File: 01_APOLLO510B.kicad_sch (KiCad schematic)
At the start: 0 parts

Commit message: fixed schematics errors
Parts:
- added C101, C102, C103, C104: 4.7uF, Capacitor_SMD:C_0201_0603Metric, symbol Device:C
- added C105: 10uF, Capacitor_SMD:C_0402_1005Metric, symbol Device:C
- added C106: 1uF, Capacitor_SMD:C_0402_1005Metric, symbol Device:C
- added C107, C108, C109, C112, C114, C117: 2.2uF, Capacitor_SMD:C_0402_1005Metric, symbol Device:C
- added C110: 4.7uF, Capacitor_SMD:C_0402_1005Metric, symbol Device:C
- added C111, C113, C115, C120, C121, C122, C123, C124, C125, C126, C127: 100nF, Capacitor_SMD:C_0402_1005Metric, symbol Device:C
- added C116: 1.0uF, Capacitor_SMD:C_0402_1005Metric, symbol Device:C
- added C118, C119: TBD <=10pF, Capacitor_SMD:C_0201_0603Metric, symbol Device:C
- added C128: 100pF, Capacitor_SMD:C_0201_0603Metric, symbol Device:C
- added L101: 2.2uH / Isat>=1A / DCR<550mR, symbol sportwatch_custom:INDUCTOR_2PIN
- added R101: 10M, Resistor_SMD:R_0402_1005Metric, symbol Device:R
- added R102, R103: 100k, Resistor_SMD:R_0402_1005Metric, symbol Device:R
- added R104, R105, R106, R107: 4.7k, Resistor_SMD:R_0402_1005Metric, symbol Device:R
- added R108: 200k, Resistor_SMD:R_0402_1005Metric, symbol Device:R
- added R109: 300k, Resistor_SMD:R_0402_1005Metric, symbol Device:R
- added R110: 10k, Resistor_SMD:R_0402_1005Metric, symbol Device:R
- added R111: 22R initial, Resistor_SMD:R_0201_0603Metric, symbol Device:R
- added U101: AP510BFA-CBR, symbol sportwatch_custom:AP510BFA-CBR
- added U102: SN74AXC8T245, symbol sportwatch_custom:SN74AXC8T245
- added U103: TXB0101DRLR, symbol sportwatch_custom:TXB0101
- added U104, U105: SN74AXC1T45, symbol sportwatch_custom:SN74AXC1T45
- added U106: PCA9306DCU, Package_SO:VSSOP-8_3.0x3.0mm_P0.65mm, symbol sportwatch_custom:PCA9306DCU
- added Y101: 32.768kHz / low-CL TBD, symbol sportwatch_custom:XTAL_2PIN
- added Y102: 48MHz / CL=8-11pF / ESR<=60R, symbol sportwatch_custom:XTAL_2PIN
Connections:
- new net ALS_INT: U101.J3 (GPIO36)
- new net APOLLO_BLE_ANT: U101.N1 (BLE_ANT)
- new net APOLLO_BLE_AVDD_PA: U101.M1 (BLE_AVDD_PA)
- new net APOLLO_BLE_ENABLE: R101.1, U101.E5 (BLE_ENABLE)
- new net APOLLO_BLE_VBAT1: C117.1, U101.A8 (BLE_VBAT1)
- new net APOLLO_BLE_XIN: U101.N6 (BLE_XIN), Y102.1 (X1)
- new net APOLLO_BLE_XOUT: U101.N7 (BLE_XOUT), Y102.2 (X2)
- new net APOLLO_LPADC_VREF: C113.1, U101.A13 (LPADC_VREF)
- new net APOLLO_LPMICBIAS: C114.1, U101.B11 (LPMICBIAS)
- new net APOLLO_RST_N: U101.H4 (RSTN)
- new net APOLLO_SIMOBUCK_SW: L101.1, U101.A1 (SIMOBUCK_SW)
- new net APOLLO_SIMOBUCK_SWSEL: L101.2, U101.A2 (SIMOBUCK_SWSEL)
- new net APOLLO_SWCLK: U101.M3 (GPIO20)
- new net APOLLO_SWDIO: U101.N3 (GPIO21)
- new net APOLLO_SWO_GPIO28: U101.L1 (GPIO28)
- new net APOLLO_VDDC: C101.1, U101.A3 (VDDC)
- new net APOLLO_VDDC_LV: C102.1, U101.B3 (VDDC_LV)
- new net APOLLO_VDDF: C103.1, U101.C2 (VDDF)
- new net APOLLO_VDDS: C104.1, U101.C1 (VDDS)
- new net APOLLO_XI32: C118.1, U101.B5 (XI), Y101.1 (X1)
- new net APOLLO_XO32: C119.1, U101.A4 (XO), Y101.2 (X2)
- new net BARO_INT: U101.F13 (GPIO37)
- new net BTN_BACK_N: U101.F11 (GPIO39)
- new net BTN_DOWN_N: U101.C4 (GPIO19)
- new net BTN_LIGHT_N: U101.G5 (GPIO17)
- new net BTN_START_N: U101.G13 (GPIO38)
- new net BTN_UP_N: U101.F5 (GPIO18)
- new net DISP_LS_OE_N: R102.2, U101.H1 (GPIO95), U102.22 (~{OE})
- new net DISP_QSPI_CLK: U102.21 (B1)
- new net DISP_QSPI_CS: U102.20 (B2)
- new net DISP_QSPI_IO0: U103.4 (B)
- new net DISP_QSPI_IO0_OE: R103.1, U101.H2 (GPIO96), U103.5 (OE)
- new net DISP_QSPI_IO1: U102.19 (B3)
- new net DISP_QSPI_IO2: U102.18 (B4)
- new net DISP_QSPI_IO3: U102.17 (B5)
- new net DISP_RST: U102.16 (B6)
- new net DISP_TE: U104.4 (B)
- new net DISP_VCI_EN: U102.15 (B7)
- new net EMMC_CLK: R111.2
- new net EMMC_CMD: U101.K8 (GPIO160)
- new net EMMC_DAT0: U101.H10 (GPIO84)
- new net EMMC_DAT1: U101.J10 (GPIO85)
- new net EMMC_DAT2: U101.K10 (GPIO86)
- new net EMMC_DAT3: U101.L9 (GPIO87)
- new net EMMC_DAT4: U101.H7 (GPIO156)
- new net EMMC_DAT5: U101.J7 (GPIO157)
- new net EMMC_DAT6: U101.K7 (GPIO158)
- new net EMMC_DAT7: U101.L8 (GPIO159)
- new net EMMC_RST_N: U101.C10 (GPIO51)
- new net ENV_I2C_SCL: U101.K3 (GPIO34)
- new net ENV_I2C_SDA: U101.J4 (GPIO35)
- new net GND: C101.2, C102.2, C103.2, C104.2, C105.2, C106.2, C107.2, C108.2, C109.2, C110.2, C111.2, C112.2, C113.2, C114.2, C115.2, C116.2, C117.2, C118.2, C119.2, C120.2, C121.2, C122.2, C123.2, C124.2, C125.2, C126.2, C127.2, C128.2, R101.2, R103.2, R109.2, U101.A6 (BLE_VSS_DCDC), U101.A7 (BLE_SW_DCDC), U101.B2 (VSSP), U101.B4 (VSSA), U101.C12 (VSSAUDA), U101.E1 (BLE_VSS1), U101.K11 (VSS), U101.L10 (VDDUSB0P9), U101.M2 (BLE_AVSS_ANT), U101.N10 (VSSAUSB), U101.N11 (VDD18), U101.N12 (VSS18), U101.N2 (BLE_AVSS_RF), U101.N9 (VDDUSB33), U102.12 (GND1), U102.13 (GND2), U103.2 (GND), U104.2 (GND), U104.5 (DIR), U105.2 (GND), U105.5 (DIR), U106.1 (GND)
- new net GNSS_EXTINT: U101.G12 (GPIO43)
- new net GNSS_TIMEPULSE: U101.E11 (GPIO45)
- new net GNSS_UART_RX: U101.C11 (GPIO46)
- new net GNSS_UART_TX: U101.F12 (GPIO44)
- new net HAPTIC_I2C_SCL: U101.K1 (GPIO47)
- new net HAPTIC_I2C_SDA: U101.J2 (GPIO48)
- new net HAPTIC_NRST: U101.J1 (GPIO49)
- new net HAPTIC_TRIG_INTZ: U101.D10 (GPIO57)
- new net IMU_INT1: U101.D7 (GPIO14)
- new net IMU_INT2: U101.H5 (GPIO16)
- new net IMU_SPI_CS: U101.D6 (GPIO11)
- new net IMU_SPI_MISO: U101.C6 (GPIO10)
- new net IMU_SPI_MOSI: U101.B6 (GPIO9)
- new net IMU_SPI_SCK: U101.D5 (GPIO8)
- new net MAG_I2C_SCL: U101.L6 (GPIO5)
- new net MAG_I2C_SDA: U101.K6 (GPIO6)
- new net MAG_INT: U101.J6 (GPIO7)
- new net MCU_DISP_QSPI_CLK_1V8: U101.D4 (GPIO102), U102.3 (A1)
- new net MCU_DISP_QSPI_CS_1V8: U101.F4 (GPIO99), U102.4 (A2)
- new net MCU_DISP_QSPI_IO0_1V8: U101.G3 (GPIO100), U103.3 (A)
- new net MCU_DISP_QSPI_IO1_1V8: U101.E4 (GPIO101), U102.5 (A3)
- new net MCU_DISP_QSPI_IO2_1V8: U101.F3 (GPIO103), U102.6 (A4)
- new net MCU_DISP_QSPI_IO3_1V8: U101.C3 (GPIO104), U102.7 (A5)
- new net MCU_DISP_RST_1V8: U101.L11 (GPIO83), U102.8 (A6)
- new net MCU_DISP_TE_1V8: U101.D11 (GPIO50), U104.3 (A)
- new net MCU_DISP_VCI_EN_1V8: U101.H3 (GPIO98), U102.9 (A7)
- new net MCU_EMMC_CLK: R111.1, U101.K9 (GPIO88)
- new net MCU_TOUCH_INT_1V8: U101.K2 (GPIO33), U105.3 (A)
- new net MCU_TOUCH_RST_1V8: U101.E10 (GPIO41), U102.10 (A8)
- new net MCU_TOUCH_SCL_1V8: R104.2, U101.K4 (GPIO31), U106.3 (SCL1)
- new net MCU_TOUCH_SDA_1V8: R105.2, U101.L3 (GPIO32), U106.4 (SDA1)
- new net PPG1_CS_N: U101.D9 (GPIO24)
- new net PPG1_INT_N: U101.D8 (GPIO22)
- new net PPG2_CS_N: U101.M5 (GPIO29)
- new net PPG2_INT_N: U101.C8 (GPIO23)
- new net PPG_SAMPLE_SYNC: U101.H13 (GPIO42)
- new net PPG_SPI_MISO: U101.L7 (GPIO27)
- new net PPG_SPI_MOSI: U101.L5 (GPIO26)
- new net PPG_SPI_SCLK: U101.K5 (GPIO25)
- new net SYS_3V3: C121.1, C123.1, C125.1, C127.1, R106.1, R107.1, R108.1, R110.1, U102.23 (VCCB1), U102.24 (VCCB2), U103.6 (VCCB), U104.6 (VCCB), U105.6 (VCCB)
- new net TOUCH_I2C_VREF2: C128.1, R108.2, U106.7 (VREF2), U106.8 (EN)
- new net TOUCH_INT: R110.2, U105.4 (B)
- new net TOUCH_RST: U102.14 (B8)
- new net TOUCH_SCL: R106.2, U106.6 (SCL2)
- new net TOUCH_SDA: R107.2, U106.5 (SDA2)
- new net VOUT1_1V8: C105.1, C106.1, C107.1, C108.1, C109.1, C110.1, C111.1, C112.1, C115.1, C116.1, C120.1, C122.1, C124.1, C126.1, R102.1, R104.1, R105.1, R109.1, U101.B1 (VDDP), U101.B12 (VDDAUDA), U101.B13 (VDDH), U101.C13 (VDDH2), U101.C5 (VDDA), U101.D1 (VDDH1), U101.E13 (BLE_VIO), U101.F1 (BLE_VCC), U101.G1 (BLE_VBAT2), U101.G10 (VDDH4), U101.H12 (VDDH3), U102.1 (VCCA), U102.11 (DIR2), U102.2 (DIR1), U103.1 (VCCA), U104.1 (VCCA), U105.1 (VCCA), U106.2 (VREF1)
- new net WIFI_BUCKEN: U101.F10 (GPIO69)
- new net WIFI_COEX_GRANT: U101.D13 (GPIO40)
- new net WIFI_COEX_REQ: U101.G11 (GPIO73)
- new net WIFI_COEX_STATUS: U101.K12 (GPIO71)
- new net WIFI_HOST_IRQ: U101.M12 (GPIO68)
- new net WIFI_IOVDD_EN: U101.J11 (GPIO70)
- new net WIFI_QSPI_CLK: U101.M11 (GPIO72)
- new net WIFI_QSPI_CS: U101.D12 (GPIO199)
- new net WIFI_QSPI_IO0: U101.H11 (GPIO64)
- new net WIFI_QSPI_IO1: U101.J13 (GPIO65)
- new net WIFI_QSPI_IO2: U101.L12 (GPIO66)
- new net WIFI_QSPI_IO3: U101.J12 (GPIO67)
- no-connect marks 0 -> 36
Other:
- note added: "01_APOLLO510B — SYSTEM MCU / FINAL SIGNAL ALLOCATION — REV A"
- note added: "32.768kHz crystal is kept for accurate RTC/timekeeping; exact crystal + load caps are selected in BOM/footprint pass. 48MHz BLE crystal uses on-chip tuning; no external load caps shown."
- note added: "All VDDP/VDDA/VDDH rails are 1.8V. VDDH1-4 are also 1.8V so every unshifted peripheral bus is 1.8V. SYS_3V3 is only used on the display/touch side of translators."
- note added: "BLE CONTROLLER — VOLTAGE MULTIPLIER MODE @ 1.8V"
- note added: "BLE controller is voltage-multiplier mode: A7 BLE_SW_DCDC grounded; VIO/VBAT2/VCC=1.8V; A8 VBAT1 has 2.2uF. This avoids a second BLE DCDC inductor."
- note added: "BLE_SW_DCDC is grounded in voltage-multiplier mode. BLE_VBAT2, BLE_VCC and BLE_VIO are all 1.8V; BLE_ENABLE E5 has the required ~10M pull-down."
- note added: "C105=VDDP 10uF; C106=VDDA 1uF; C107=VDDH 2.2uF; C108=VDDH1 2.2uF; C109=VDDH2 2.2uF; C110=VDDH3 4.7uF; C111=VDDH4 100nF; C112=VDDAUDA 2.2uF."
- note added: "CO5300 command reads return on QSPI SIO0. U103 is TXB0101 auto-direction; 1.8V-side max data rate is 60Mbps versus CO5300 max 50MHz QSPI write clock / 10MHz read clock."
- note added: "DISPLAY + TOUCH LEVEL TRANSLATION — REQUIRED: APOLLO GPIO=1.8V, SELECTED MODULE I/O=3.3V"
- note added: "Display uses dedicated DISP_QSPI functions on GPIO100-104, GPIO83 reset, GPIO50 TE, GPIO99 CS (GPIO), GPIO98 VCI_EN. GPIO96 controls U103 OE; GPIO95 controls U102 OE."
- note added: "GPIO15/J5 is internally used as BLE reference clock and is NC. RESERVED balls H8/H9/J8/J9/M7/M8 are NC. USB data/MIPI pads are NC; unused USB/MIPI supply rails are grounded per Ambiq guidance."
- note added: "Native KiCad ERC must be run after final hierarchical export because child-sheet labels are not cross-sheet connections yet."
- note added: "PIN MUX: eMMC reserves SDIF0 GPIO84-88 + GPIO156-160; do not reassign. R111 is at Apollo end of CLK."
- note added: "POWER / SIMO / CLOCK SUPPORT"
- note added: "R111 is the eMMC clock source terminator and belongs physically next to Apollo GPIO88; 22R is an initial SI value."
- note added: "Selected ZC-A1D43W-046 module specifies 3.3V QSPI and touch I/O. Apollo GPIO rails are 1.8V here, so level translation is mandatory. Keep 03_DISPLAY R301/R302 DNP because U106 block provides high-side I2C pull-ups."
- note added: "U101 pin map = exact AP510BFA-CBR 153-ball package. Gray/unpopulated package positions are omitted; RESERVED balls and GPIO15 are explicitly NC."
- note added: "Wi-Fi uses MSPI0 GPIO64-73 plus GPIO199 CS; all on 1.8V VDDH3 domain. nRF7002 IOVDD is also 1.8V."
- title: (none) -> Rev-A — Apollo510B MCU / System Integration

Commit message: refactor(kicad): integrate Rev-A hierarchy and libraries
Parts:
- U106: footprint Package_SO:VSSOP-8_3.0x3.0mm_P0.65mm -> Package_SO:VSSOP-8_2.3x2mm_P0.5mm

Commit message: feat(kicad): assign and audit Rev-A footprints
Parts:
- L101: footprint (none) -> Inductor_SMD:L_0603_1608Metric
- U101: footprint (none) -> sportwatch_custom:BGA-153_5.6x5.6mm_Layout13x13_P0.4mm_Ball0.25mm_Pad0.22mm_NSMD
- U102: footprint (none) -> sportwatch_custom:Texas_RHL0024A
- U103, U104, U105: footprint (none) -> Package_TO_SOT_SMD:SOT-563
- Y101: footprint (none) -> Crystal:Crystal_SMD_2012-2Pin_2.0x1.2mm
- Y102: footprint (none) -> sportwatch_custom:Crystal_1612-2Pin_1.6x1.2mm
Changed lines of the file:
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@@
 			)
 		)
-		(property "Footprint" ""
+		(property "Footprint" "sportwatch_custom:BGA-153_5.6x5.6mm_Layout13x13_P0.4mm_Ball0.25mm_Pad0.22mm_NSMD"
 			(at 153 148 0)
 			(hide yes)
@@
 			)
 		)
-		(property "Footprint" ""
+		(property "Footprint" "Package_TO_SOT_SMD:SOT-563"
 			(at 400 222 0)
 			(hide yes)
@@
 			)
 		)
-		(property "Footprint" ""
+		(property "Footprint" "Package_TO_SOT_SMD:SOT-563"
 			(at 350 222 0)
 			(hide yes)
@@
 			)
 		)
-		(property "Footprint" ""
+		(property "Footprint" "Package_TO_SOT_SMD:SOT-563"
 			(at 300 222 0)
 			(hide yes)
@@
 			)
 		)
-		(property "Footprint" ""
+		(property "Footprint" "Inductor_SMD:L_0603_1608Metric"
 			(at 285 30 0)
 			(hide yes)
@@
 			)
 		)
-		(property "Footprint" ""
+		(property "Footprint" "sportwatch_custom:Crystal_1612-2Pin_1.6x1.2mm"
 			(at 390 104 0)
 			(hide yes)
@@
 			)
 		)
-		(property "Footprint" ""
+		(property "Footprint" "Crystal:Crystal_SMD_2012-2Pin_2.0x1.2mm"
 			(at 340 104 0)
 			(hide yes)
@@
 			)
 		)
-		(property "Footprint" ""
+		(property "Footprint" "sportwatch_custom:Texas_RHL0024A"
 			(at 300 190 0)
 			(hide yes)

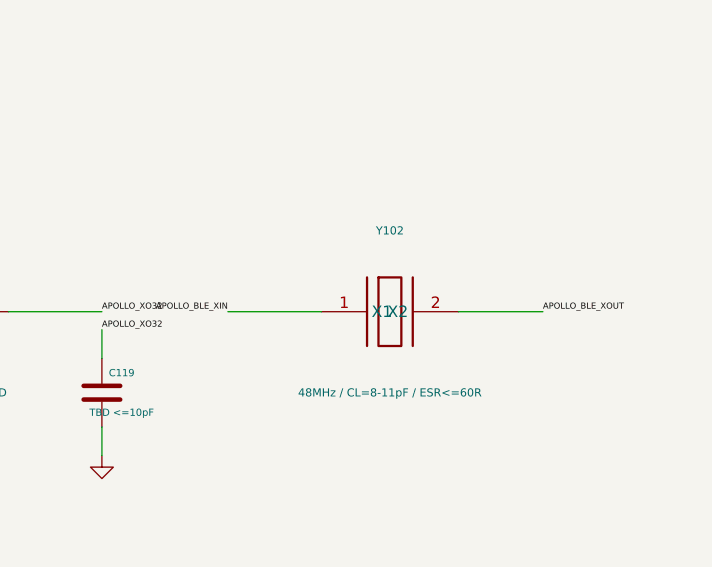
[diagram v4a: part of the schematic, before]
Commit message: fix(pcba): resolve post-footprint freeze sanity items and freeze footprints
- Resolve Flatpak KICAD10_SYMBOL_DIR path discrepancy, reducing lib_symbol_issues to 0
- Re-audit Y1 and Y102 crystals against NDK NX1612SA; ground pads 2/4 for RF shield
- Reclassify SW1..SW5, J201, and J202 as Class C pending mechanical enclosure freeze
- Verify native ERC (0 errors), 83 interfaces (checked=83 mismatches=0), and 0 unintended net changes
- Add docs/project/post_footprint_freeze_sanity.md with FOOTPRINT FREEZE: PASS
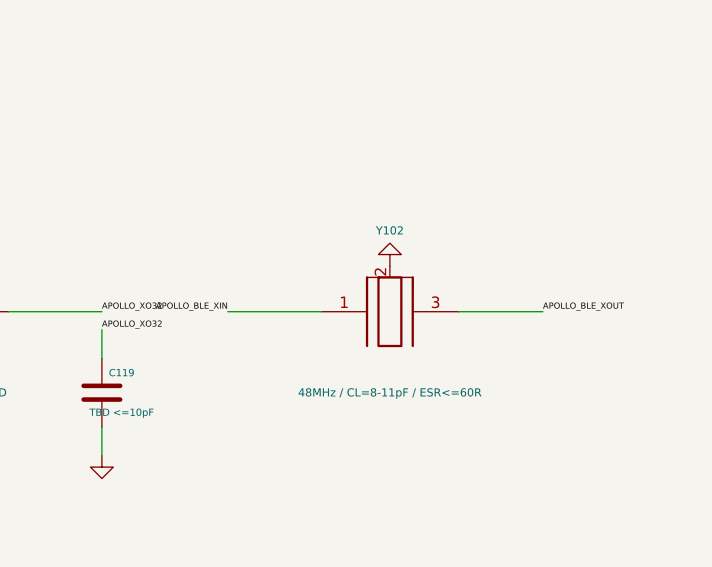
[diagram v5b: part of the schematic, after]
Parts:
- Y102: footprint sportwatch_custom:Crystal_1612-2Pin_1.6x1.2mm -> sportwatch_custom:Crystal_1612-4Pin_1.6x1.2mm; symbol sportwatch_custom:XTAL_2PIN -> sportwatch_custom:Crystal_1612-4Pin_GND
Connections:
- net APOLLO_BLE_XOUT: now also Y102.3; no longer Y102.2 (X2)
- net GND: now also Y102.2 (GND), Y102.4 (GND)
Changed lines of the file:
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@@
 	)
 	(symbol
-		(lib_id "sportwatch_custom:XTAL_2PIN")
+		(lib_id "sportwatch_custom:Crystal_1612-4Pin_GND")
 		(at 390 104 0)
 		(unit 1)
@@
 			)
 		)
-		(property "Footprint" "sportwatch_custom:Crystal_1612-2Pin_1.6x1.2mm"
+		(property "Footprint" "sportwatch_custom:Crystal_1612-4Pin_1.6x1.2mm"
 			(at 390 104 0)
 			(hide yes)
@@
 		(pin "1"
 		)
+		(pin "3"
+		)
 		(pin "2"
+		)
+		(pin "4"
 		)
 		(instances
@@
 					(unit 1)
 				)
+			)
+		)
+	)
+	(symbol
+		(lib_id "power:GND")
+		(at 390 98.92 180)
+		(unit 1)
+		(body_style 1)
+		(exclude_from_sim no)
+		(in_bom yes)
+		(on_board yes)
+		(in_pos_files yes)
+		(dnp no)
+		(property "Reference" "#PWR0191"
+			(at 390 98.92 0)
+			(hide yes)
+			(show_name no)
+			(do_not_autoplace no)
+			(effects
+				(font
+					(size 1.27 1.27)
+				)
+			)
+		)
+		(property "Value" "GND"
+			(at 390 102.73 0)
+			(hide yes)
+			(show_name no)
+			(do_not_autoplace no)
+			(effects
+				(font
+					(size 1.27 1.27)
+				)
+			)
+		)
+		(property "Footprint" ""
+			(at 390 98.92 0)
+			(hide yes)
+			(show_name no)
+			(do_not_autoplace no)
+			(effects
+				(font
+					(size 1.27 1.27)
+				)
+			)
+		)
+		(property "Datasheet" ""
+			(at 390 98.92 0)
+			(hide yes)
+			(show_name no)
+			(do_not_autoplace no)
+			(effects
+				(font
+					(size 1.27 1.27)
+				)
+			)
+		)
+		(property "Description" ""
+			(at 390 98.92 0)
+			(hide yes)
+			(show_name no)
+			(do_not_autoplace no)
+			(effects
+				(font
+					(size 1.27 1.27)
+				)
+			)
+		)
+		(pin "1"
+		)
+		(instances
+			(project "sportwatch_revA"
+				(path "/063f9d99-6c07-44cf-ba32-e33897e06972/32562f69-31ef-430f-b0b9-492916776cb7"
+					(reference "#PWR0191")
+					(unit 1)
+				)

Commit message: fix(pcb): Round 3 foundation correction — 0 DRC errors, stacked microvias, PPG ECO & guards
- Eliminate 24 committed DRC errors by refilling all zones and committing refilled state
- Rebuild 12 L1->L3 skip microvias as 24 stackup-compliant stacked L1->L2 + L2->L3 microvias (VIPPO IPC-4761 Type VII)
- Harmonize HighSpeed_50R track width to 0.100 mm across .kicad_pro, .kicad_dru, and live copper
- Execute controlled schematic ECO swapping D413 and D424 detector channels, eliminating Jordan curve crossing
- Route all 4 PPG detector channels pad-to-pad on B.Cu with continuous dedicated PD_GND ground guards
- Close schematic residuals: Y101 MPN ABS07-32.768KHZ-6-T and 8.2pF load caps, cite primary sources for Y102 and Y1 on-chip trim, cite u-blox manual for U8 VCC_RF NC
- Formally defer staged passives (eMMC interface, PPG VLED, C206) with documented reserved placement corridors
- Document comprehensive Round 3 report and update Apollo/eMMC escape matrices and AGENT_HANDOFF.md
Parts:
- C118, C119: value TBD <=10pF -> 8.2pF
- Y101: value 32.768kHz / low-CL TBD -> ABS07-32.768KHZ-6-T
- Y102: value 48MHz / CL=8-11pF / ESR<=60R -> NX1612SA-48M-EXS00A-CS14265
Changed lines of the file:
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@@
 			)
 		)
-		(property "Value" "TBD <=10pF"
+		(property "Value" "8.2pF"
 			(at 324.2 115.2 0)
 			(show_name no)
@@
 			)
 		)
-		(property "Value" "48MHz / CL=8-11pF / ESR<=60R"
+		(property "Value" "NX1612SA-48M-EXS00A-CS14265"
 			(at 390 113 0)
 			(show_name no)
@@
 			)
 		)
-		(property "Value" "32.768kHz / low-CL TBD"
+		(property "Value" "ABS07-32.768KHZ-6-T"
 			(at 340 113 0)
 			(show_name no)
@@
 			)
 		)
-		(property "Value" "TBD <=10pF"
+		(property "Value" "8.2pF"
 			(at 360.2 115.2 0)
 			(show_name no)

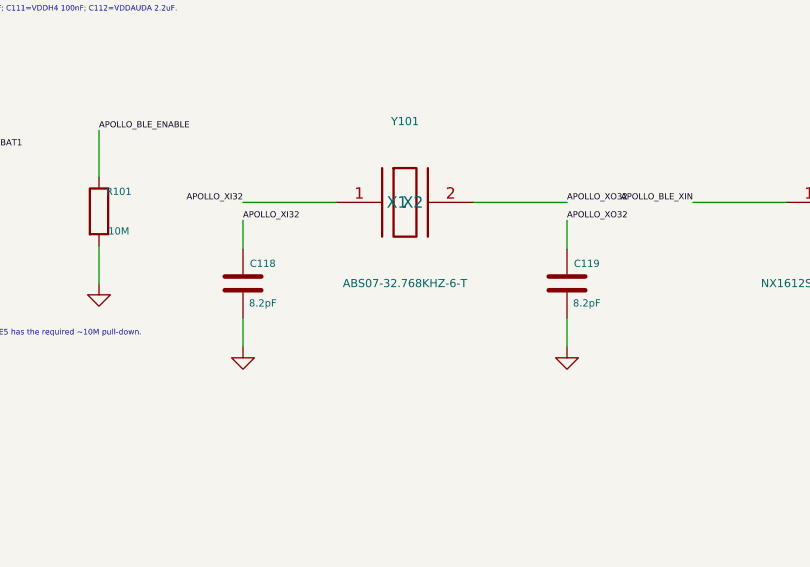
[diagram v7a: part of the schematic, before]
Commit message: fix(pcb): foundation correction round 4 closure
- Y101: select Abracon ABS06-32.768KHZ-6-1-T (2012-class SMD crystal) matching 2012 footprint
- Y101/C118/C119: rotate Y101 180 deg to align XO32 West and XI32 East; uncrossed planar routing
- Parity: synchronize C118, C119, Y101, Y102, Y1 values between schematic and PCB (0 mismatches)
- PPG guards: close NT401.2 and NT402.2 to In6.Cu GND plane via B.Cu microvias (4 channels complete)
- Rules: reconcile HighSpeed_50R track_width to 0.100 mm in .kicad_pro; refine *1V8* to *VOUT*1V8*
- GNSS: update note to cite MAX-F10S Integration Manual UBXDOC-963802114-12892 R01 and south RF_IN
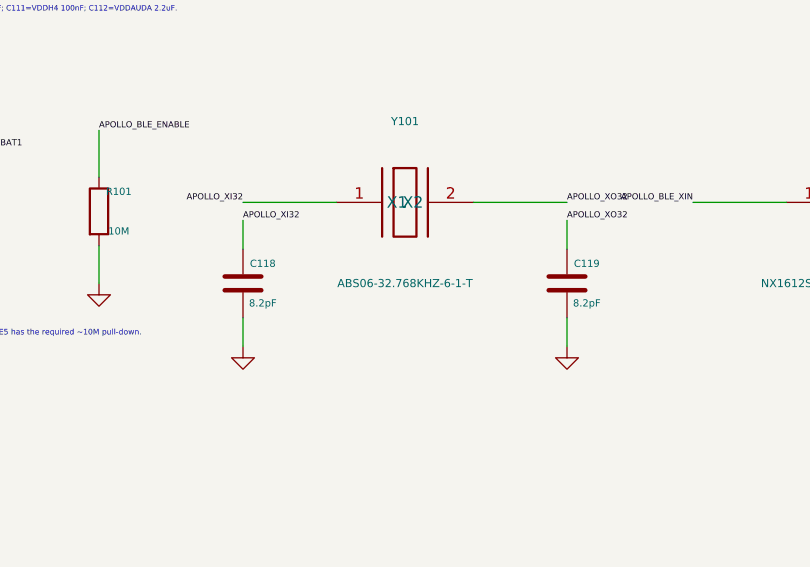
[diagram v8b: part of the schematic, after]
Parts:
- Y101: value ABS07-32.768KHZ-6-T -> ABS06-32.768KHZ-6-1-T
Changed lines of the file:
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@@
 			)
 		)
-		(property "Value" "ABS07-32.768KHZ-6-T"
+		(property "Value" "ABS06-32.768KHZ-6-1-T"
 			(at 340 113 0)
 			(show_name no)
@@
 			)
 		)
-		(property "Description" "32.768kHz RTC crystal; choose CL compatible with <=10pF external cap per pin"
+		(property "Description" "32.768kHz RTC crystal; 6pF CL, 90k ESR, 2012 package compatible with Apollo510B"
 			(at 340 104 0)
 			(hide yes)
